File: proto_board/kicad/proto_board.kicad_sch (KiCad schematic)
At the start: 1 part, among them J1 pcie_98

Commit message: Work in progress. Backlane kicad.
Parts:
- added H1, H2: Bracket Hole, MountingHole:MountingHole_3.2mm_M3_Pad_Via, symbol Mechanical:MountingHole
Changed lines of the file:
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@@
   (symbol (lib_id "power:+5V") (at 320.04 64.77 0) (unit 1)
     (in_bom yes) (on_board yes) (dnp no) (fields_autoplaced)
-    (property "Reference" "#PWR02" (at 320.04 68.58 0)
+    (property "Reference" "#PWR03" (at 320.04 68.58 0)
       (effects (font (size 1.27 1.27)) hide)
     )
@@
       (project "proto_board"
         (path "/0dcd9c8c-bd5a-437f-856e-101fb6cf8b66"
-          (reference "#PWR02") (unit 1)
+          (reference "#PWR03") (unit 1)
+        )
+      )
+    )
+  )
+  (symbol (lib_id "Mechanical:MountingHole") (at 264.16 30.48 0) (unit 1)
+    (in_bom yes) (on_board yes) (dnp no) (fields_autoplaced)
+    (property "Reference" "H1" (at 266.7 29.8363 0)
+      (effects (font (size 1.27 1.27)) (justify left))
+    )
+    (property "Value" "Bracket Hole" (at 266.7 31.7573 0)
+      (effects (font (size 1.27 1.27)) (justify left))
+    )
+    (property "Footprint" "MountingHole:MountingHole_3.2mm_M3_Pad_Via" (at 264.16 30.48 0)
+      (effects (font (size 1.27 1.27)) hide)
+    )
+    (property "Datasheet" "~" (at 264.16 30.48 0)
+      (effects (font (size 1.27 1.27)) hide)
+    )
+    (instances
+      (project "proto_board"
+        (path "/0dcd9c8c-bd5a-437f-856e-101fb6cf8b66"
+          (reference "H1") (unit 1)
         )
       )
@@
   (symbol (lib_id "power:+3.3V") (at 314.96 64.77 0) (unit 1)
     (in_bom yes) (on_board yes) (dnp no) (fields_autoplaced)
-    (property "Reference" "#PWR03" (at 314.96 68.58 0)
+    (property "Reference" "#PWR01" (at 314.96 68.58 0)
       (effects (font (size 1.27 1.27)) hide)
     )
@@
       (project "proto_board"
         (path "/0dcd9c8c-bd5a-437f-856e-101fb6cf8b66"
-          (reference "#PWR03") (unit 1)
+          (reference "#PWR01") (unit 1)
+        )
+      )
+    )
+  )
+  (symbol (lib_id "Mechanical:MountingHole") (at 264.16 35.56 0) (unit 1)
+    (in_bom yes) (on_board yes) (dnp no) (fields_autoplaced)
+    (property "Reference" "H2" (at 266.7 34.9163 0)
+      (effects (font (size 1.27 1.27)) (justify left))
+    )
+    (property "Value" "Bracket Hole" (at 266.7 36.8373 0)
+      (effects (font (size 1.27 1.27)) (justify left))
+    )
+    (property "Footprint" "MountingHole:MountingHole_3.2mm_M3_Pad_Via" (at 264.16 35.56 0)
+      (effects (font (size 1.27 1.27)) hide)
+    )
+    (property "Datasheet" "~" (at 264.16 35.56 0)
+      (effects (font (size 1.27 1.27)) hide)
+    )
+    (instances
+      (project "proto_board"
+        (path "/0dcd9c8c-bd5a-437f-856e-101fb6cf8b66"
+          (reference "H2") (unit 1)
         )
       )
@@
   (symbol (lib_id "proto_board:GND") (at 314.96 68.58 0) (unit 1)
     (in_bom yes) (on_board yes) (dnp no) (fields_autoplaced)
-    (property "Reference" "#PWR01" (at 314.96 74.93 0)
+    (property "Reference" "#PWR02" (at 314.96 74.93 0)
       (effects (font (size 1.27 1.27)) hide)
     )
@@
       (project "proto_board"
         (path "/0dcd9c8c-bd5a-437f-856e-101fb6cf8b66"
-          (reference "#PWR01") (unit 1)
+          (reference "#PWR02") (unit 1)
         )
       )

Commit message: Proto board work in progress.
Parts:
- removed H1, H2: Bracket Hole, MountingHole:MountingHole_3.2mm_M3_Pad_Via, symbol Mechanical:MountingHole
- added J2, J3: Conn_02x25_Odd_Even, Connector_PinHeader_2.00mm:PinHeader_2x25_P2.00mm_Vertical_SMD, symbol Connector_Generic:Conn_02x25_Odd_Even
- J1: symbol proto_board:pcie_96 -> proto_board:pcie_98
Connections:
- new net A1: J1.A1 (Pin_a1), J2.1 (Pin_1)
- new net A2: J1.A2 (Pin_a2), J2.2 (Pin_2)
- new net A3: J1.A3 (Pin_a3), J2.3 (Pin_3)
- new net A4: J1.A4 (Pin_a4), J2.4 (Pin_4)
- new net B1: J1.B1 (Pin_b1), J3.1 (Pin_1)
- new net B2: J1.B2 (Pin_b2), J3.2 (Pin_2)
- new net B3: J1.B3 (Pin_b3), J3.3 (Pin_3)
- new net B4: J1.B4 (Pin_b4), J3.4 (Pin_4)
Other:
- note added: "TODO: Revisit the two short edge connector pads."
- note removed: "TODO: Add bypass capacitors"
- moved on the sheet: J1

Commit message: Cleaned up the outline and fanout of the proto board.
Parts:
- J2, J3: footprint Connector_PinHeader_2.00mm:PinHeader_2x25_P2.00mm_Vertical_SMD -> proto_board:PinHeader_2x25_P2.00mm_Vertical_SMD
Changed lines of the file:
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@@
       (effects (font (size 1.27 1.27)))
     )
-    (property "Footprint" "Connector_PinHeader_2.00mm:PinHeader_2x25_P2.00mm_Vertical_SMD" (at 294.64 111.76 0)
+    (property "Footprint" "proto_board:PinHeader_2x25_P2.00mm_Vertical_SMD" (at 294.64 111.76 0)
       (effects (font (size 1.27 1.27)) hide)
     )
@@
       (effects (font (size 1.27 1.27)))
     )
-    (property "Footprint" "Connector_PinHeader_2.00mm:PinHeader_2x25_P2.00mm_Vertical_SMD" (at 350.52 111.76 0)
+    (property "Footprint" "proto_board:PinHeader_2x25_P2.00mm_Vertical_SMD" (at 350.52 111.76 0)
       (effects (font (size 1.27 1.27)) hide)
     )

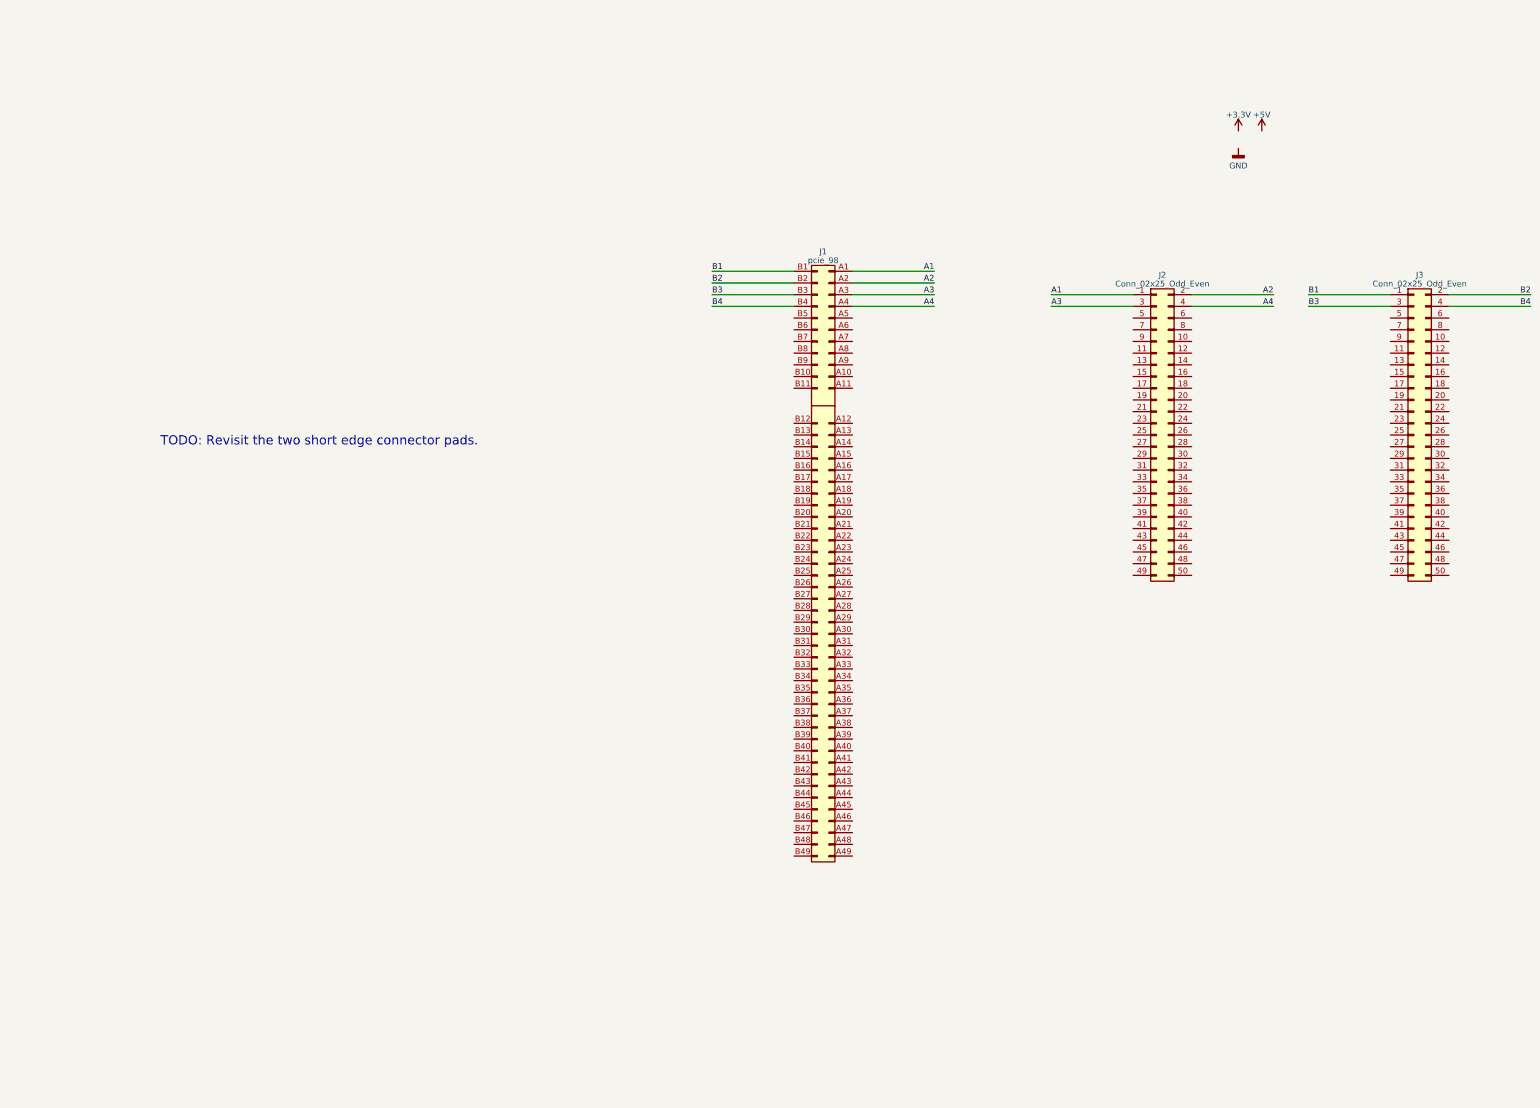
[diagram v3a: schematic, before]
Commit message: Resized the proto board and added pads grid.
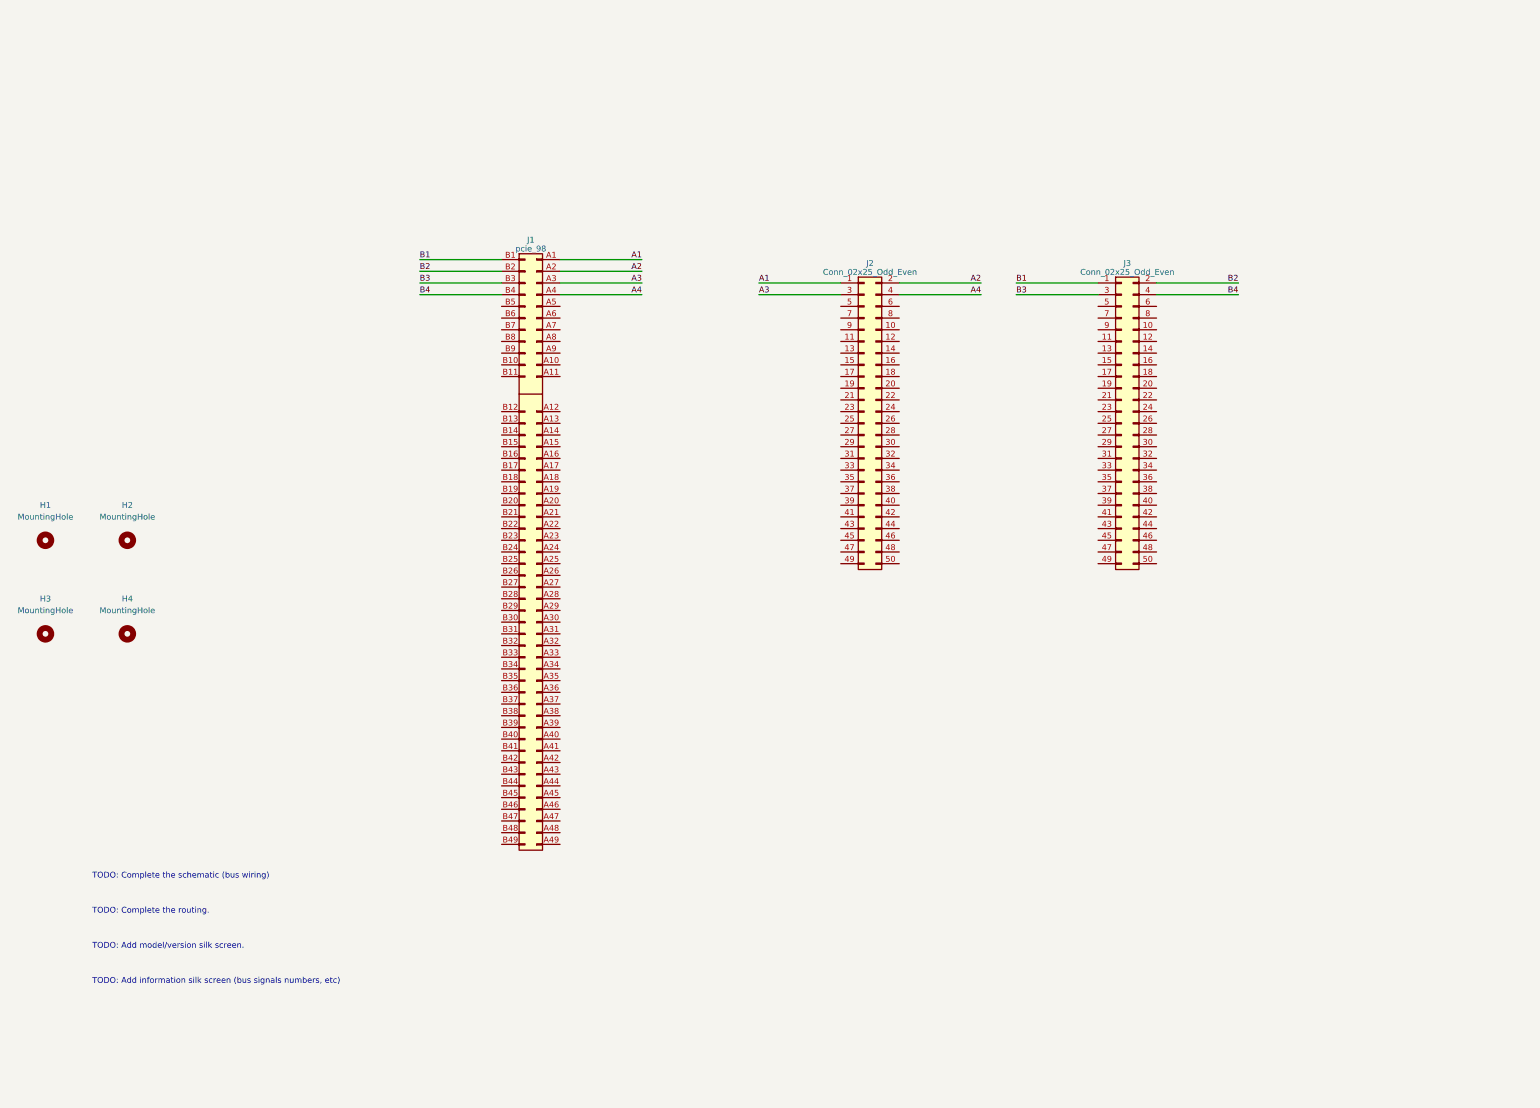
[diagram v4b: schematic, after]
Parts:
- added H1, H2, H3, H4: MountingHole, MountingHole:MountingHole_3.2mm_M3_Pad_Via, symbol Mechanical:MountingHole
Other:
- note added: "TODO: Add information silk screen (bus signals numbers, etc)"
- note added: "TODO: Add model/version silk screen."
- note added: "TODO: Complete the routing."
- note added: "TODO: Complete the schematic (bus wiring)"
- note removed: "TODO: Revisit the two short edge connector pads."
- moved on the sheet: J1, J2, J3

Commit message: More progress on the schematic. Yet to complete the connectivity.
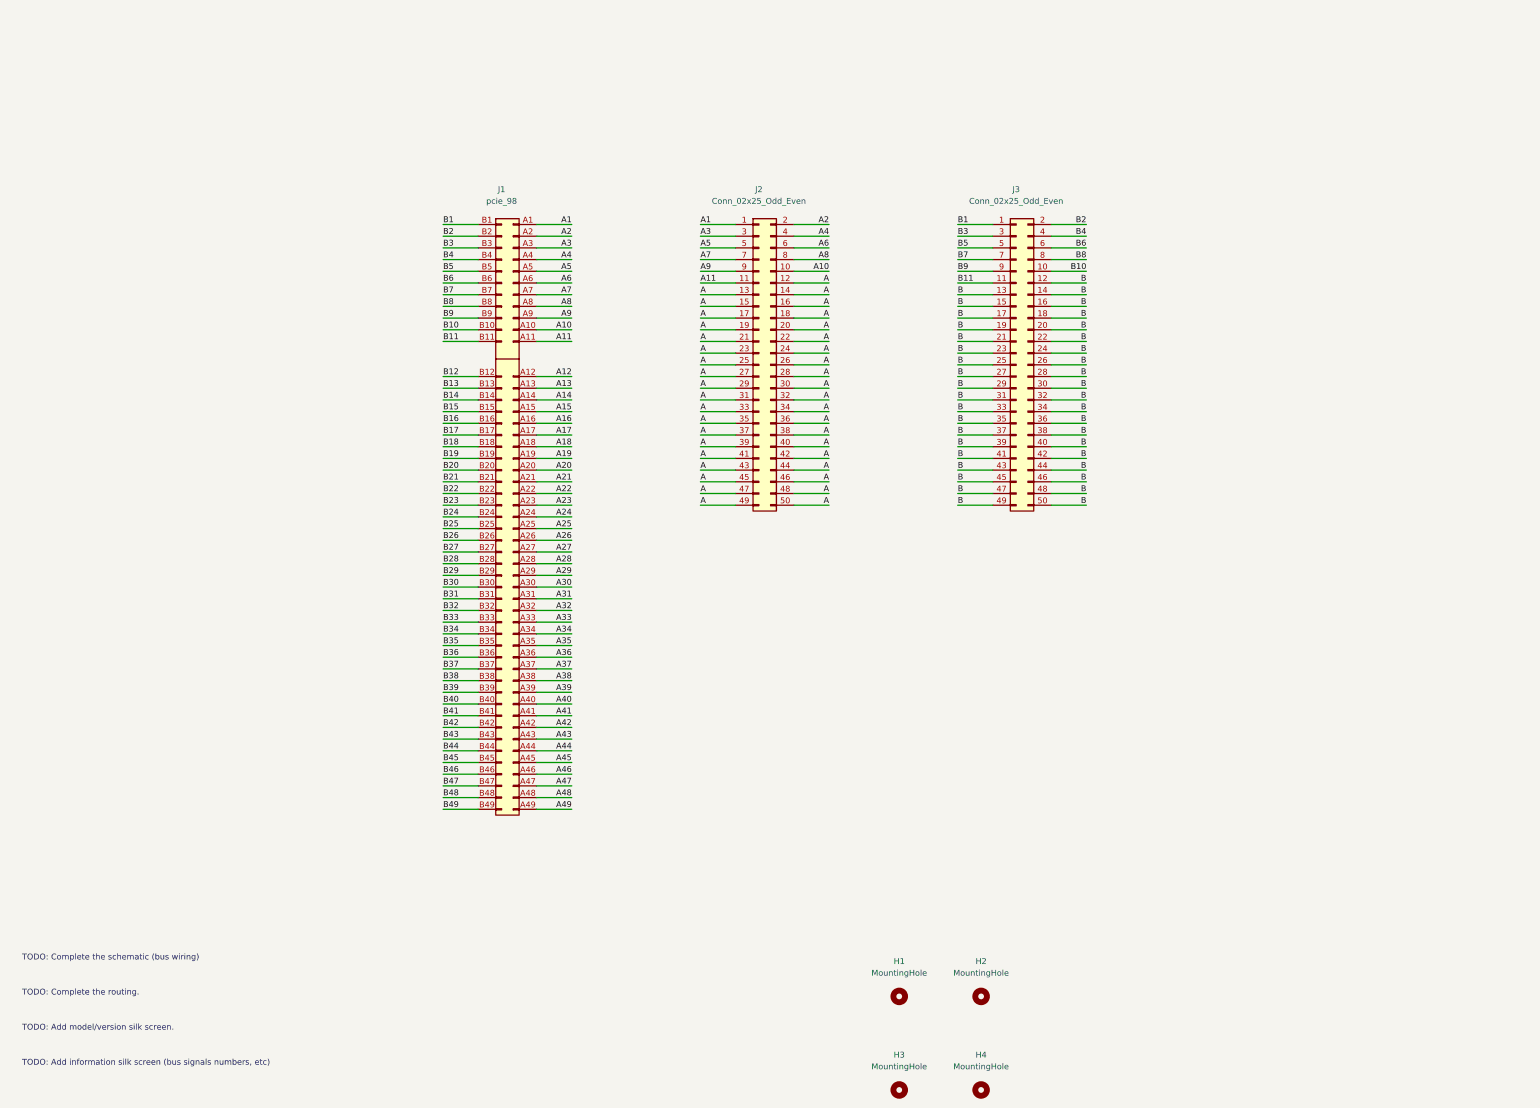
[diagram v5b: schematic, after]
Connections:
- net A10: now reaches J1.A10 (Pin_a10)
- net A10: now also J2.10 (Pin_10)
- net A11: now reaches J1.A11 (Pin_A11)
- net A11: now also J2.11 (Pin_11)
- net A12: now reaches J1.A12 (Pin_a12)
- net A13: now reaches J1.A13 (Pin_a13)
- net A14: now reaches J1.A14 (Pin_a14)
- net A15: now reaches J1.A15 (Pin_a15)
- net A16: now reaches J1.A16 (Pin_a16)
- net A17: now reaches J1.A17 (Pin_a17)
- net A18: now reaches J1.A18 (Pin_a18)
- net A19: now reaches J1.A19 (Pin_a19)
- net A20: now reaches J1.A20 (Pin_a20)
- net A21: now reaches J1.A21 (Pin_a21)
- net A22: now reaches J1.A22 (Pin_a22)
- net A23: now reaches J1.A23 (Pin_a23)
- net A24: now reaches J1.A24 (Pin_a24)
- net A25: now reaches J1.A25 (Pin_a25)
- net A26: now reaches J1.A26 (Pin_a26)
- net A27: now reaches J1.A27 (Pin_a27)
- net A28: now reaches J1.A28 (Pin_a28)
- net A29: now reaches J1.A29 (Pin_a29)
- net A30: now reaches J1.A30 (Pin_a30)
- net A31: now reaches J1.A31 (Pin_a31)
- net A32: now reaches J1.A32 (Pin_a32)
- net A33: now reaches J1.A33 (Pin_a33)
- net A34: now reaches J1.A34 (Pin_a34)
- net A35: now reaches J1.A35 (Pin_a35)
- net A36: now reaches J1.A36 (Pin_a36)
- net A37: now reaches J1.A37 (Pin_a37)
- net A38: now reaches J1.A38 (Pin_a38)
- net A39: now reaches J1.A39 (Pin_a39)
- net A40: now reaches J1.A40 (Pin_a40)
- net A41: now reaches J1.A41 (Pin_a41)
- net A42: now reaches J1.A42 (Pin_a42)
- net A43: now reaches J1.A43 (Pin_a43)
- net A44: now reaches J1.A44 (Pin_a44)
- net A45: now reaches J1.A45 (Pin_a45)
- net A46: now reaches J1.A46 (Pin_a46)
- net A47: now reaches J1.A47 (Pin_a47)
- net A48: now reaches J1.A48 (Pin_a48)
- net A49: now reaches J1.A49 (Pin_a49)
- net A5: now reaches J1.A5 (Pin_a5)
- net A5: now also J2.5 (Pin_5)
- net A6: now reaches J1.A6 (Pin_a6)
- net A6: now also J2.6 (Pin_6)
- net A7: now reaches J1.A7 (Pin_a7)
- net A7: now also J2.7 (Pin_7)
- net A8: now reaches J1.A8 (Pin_a8)
- net A8: now also J2.8 (Pin_8)
- net A9: now reaches J1.A9 (Pin_a9)
- net A9: now also J2.9 (Pin_9)
- net B10: now reaches J1.B10 (Pin_b10)
- net B10: now also J3.10 (Pin_10)
- net B11: now reaches J1.B11 (Pin_b11)
- net B11: now also J3.11 (Pin_11)
- net B12: now reaches J1.B12 (Pin_b12)
- net B13: now reaches J1.B13 (Pin_b13)
- net B14: now reaches J1.B14 (Pin_b14)
- net B15: now reaches J1.B15 (Pin_b15)
- net B16: now reaches J1.B16 (Pin_b16)
- net B17: now reaches J1.B17 (Pin_b17)
- net B18: now reaches J1.B18 (Pin_b18)
- net B19: now reaches J1.B19 (Pin_b19)
- net B20: now reaches J1.B20 (Pin_b20)
- net B21: now reaches J1.B21 (Pin_b21)
- net B22: now reaches J1.B22 (Pin_b22)
- net B23: now reaches J1.B23 (Pin_b23)
- net B24: now reaches J1.B24 (Pin_b24)
- net B25: now reaches J1.B25 (Pin_b25)
- net B26: now reaches J1.B26 (Pin_b26)
- net B27: now reaches J1.B27 (Pin_b27)
- net B28: now reaches J1.B28 (Pin_b28)
- net B29: now reaches J1.B29 (Pin_b29)
- net B30: now reaches J1.B30 (Pin_b30)
- net B31: now reaches J1.B31 (Pin_b31)
- net B32: now reaches J1.B32 (Pin_b32)
- net B33: now reaches J1.B33 (Pin_b33)
- net B34: now reaches J1.B34 (Pin_b34)
- net B35: now reaches J1.B35 (Pin_b35)
- net B36: now reaches J1.B36 (Pin_b36)
- net B37: now reaches J1.B37 (Pin_b37)
- net B38: now reaches J1.B38 (Pin_b38)
- net B39: now reaches J1.B39 (Pin_b39)
- net B40: now reaches J1.B40 (Pin_b40)
- net B41: now reaches J1.B41 (Pin_b41)
- net B42: now reaches J1.B42 (Pin_b42)
- net B43: now reaches J1.B43 (Pin_b43)
- net B44: now reaches J1.B44 (Pin_b44)
- net B45: now reaches J1.B45 (Pin_b45)
- net B46: now reaches J1.B46 (Pin_46)
- net B47: now reaches J1.B47 (Pin_b47)
- net B48: now reaches J1.B48 (Pin_b48)
- net B49: now reaches J1.B49 (Pin_b49)
- net B5: now reaches J1.B5 (Pin_b5)
- net B5: now also J3.5 (Pin_5)
- net B6: now reaches J1.B6 (Pin_b6)
- net B6: now also J3.6 (Pin_6)
- net B7: now reaches J1.B7 (Pin_b7)
- net B7: now also J3.7 (Pin_7)
- net B8: now reaches J1.B8 (Pin_b8)
- net B8: now also J3.8 (Pin_8)
- net B9: now reaches J1.B9 (Pin_b9)
- net B9: now also J3.9 (Pin_9)
- net A: now reaches J2.12 (Pin_12)
- net A: now also J2.13 (Pin_13), J2.14 (Pin_14), J2.15 (Pin_15), J2.16 (Pin_16), J2.17 (Pin_17), J2.18 (Pin_18), J2.19 (Pin_19), J2.20 (Pin_20), J2.21 (Pin_21), J2.22 (Pin_22), J2.23 (Pin_23), J2.24 (Pin_24), J2.25 (Pin_25), J2.26 (Pin_26), J2.27 (Pin_27), J2.28 (Pin_28), J2.29 (Pin_29), J2.30 (Pin_30), J2.31 (Pin_31), J2.32 (Pin_32), J2.33 (Pin_33), J2.34 (Pin_34), J2.35 (Pin_35), J2.36 (Pin_36), J2.37 (Pin_37), J2.38 (Pin_38), J2.39 (Pin_39), J2.40 (Pin_40), J2.41 (Pin_41), J2.42 (Pin_42), J2.43 (Pin_43), J2.44 (Pin_44), J2.45 (Pin_45), J2.46 (Pin_46), J2.47 (Pin_47), J2.48 (Pin_48), J2.49 (Pin_49), J2.50 (Pin_50)
- net B: now reaches J3.12 (Pin_12)
- net B: now also J3.13 (Pin_13), J3.14 (Pin_14), J3.15 (Pin_15), J3.16 (Pin_16), J3.17 (Pin_17), J3.18 (Pin_18), J3.19 (Pin_19), J3.20 (Pin_20), J3.21 (Pin_21), J3.22 (Pin_22), J3.23 (Pin_23), J3.24 (Pin_24), J3.25 (Pin_25), J3.26 (Pin_26), J3.27 (Pin_27), J3.28 (Pin_28), J3.29 (Pin_29), J3.30 (Pin_30), J3.31 (Pin_31), J3.32 (Pin_32), J3.33 (Pin_33), J3.34 (Pin_34), J3.35 (Pin_35), J3.36 (Pin_36), J3.37 (Pin_37), J3.38 (Pin_38), J3.39 (Pin_39), J3.40 (Pin_40), J3.41 (Pin_41), J3.42 (Pin_42), J3.43 (Pin_43), J3.44 (Pin_44), J3.45 (Pin_45), J3.46 (Pin_46), J3.47 (Pin_47), J3.48 (Pin_48), J3.49 (Pin_49), J3.50 (Pin_50)
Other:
- moved on the sheet: H1, H2, H3, H4, J1, J2, J3
